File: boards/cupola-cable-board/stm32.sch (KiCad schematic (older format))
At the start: 15 parts, among them J11 SWD, J12 DebugUart, U2 STM32F410CBTx, X1 ECS-3963-120-AU-TR

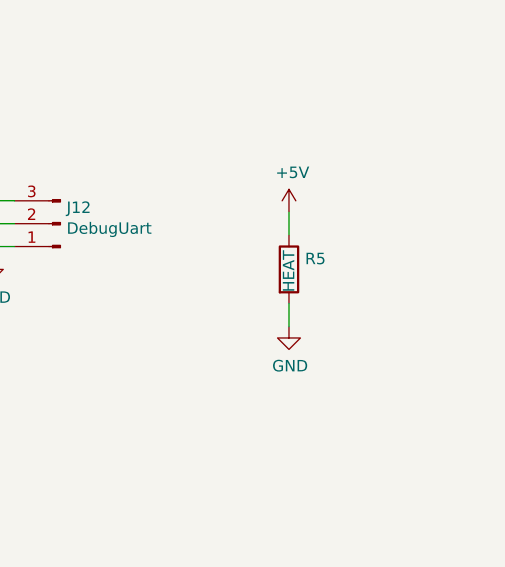
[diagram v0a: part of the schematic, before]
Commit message: cupola_cable_board: 500mA 3.3V regulator, 4 pin connector for magnetic encoder
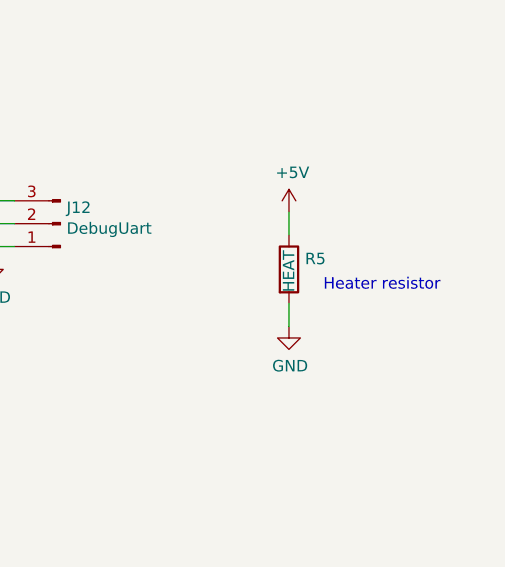
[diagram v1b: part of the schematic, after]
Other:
- note added: "Heater resistor"
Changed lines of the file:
@@
 Wire Wire Line
 	8400 2100 8400 2200
+Text Notes 8550 2050 0    50   ~ 0
+Heater resistor
 $EndSCHEMATC

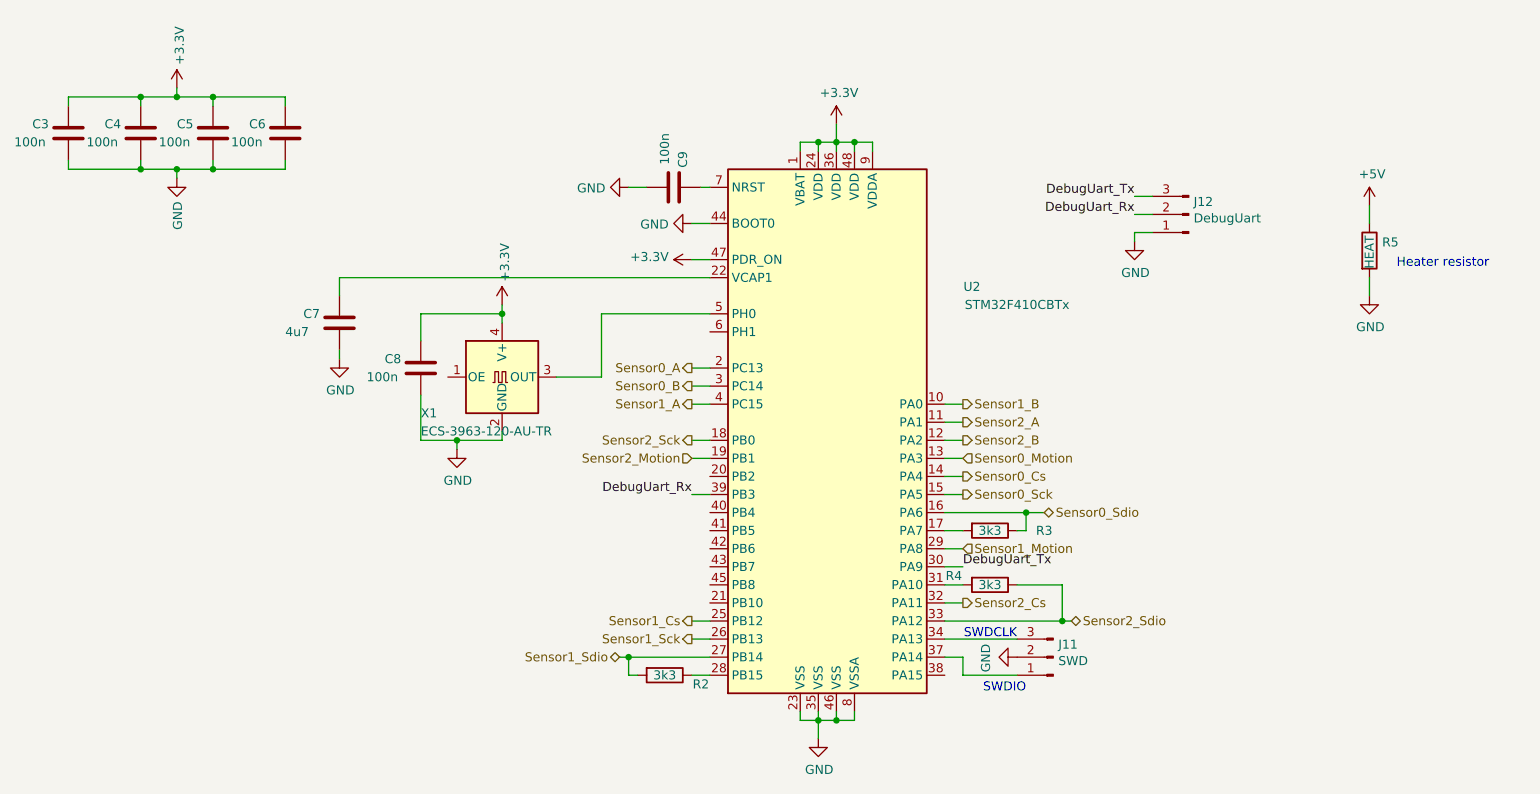
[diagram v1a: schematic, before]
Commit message: cupola board: Swap STM pins for easier layout
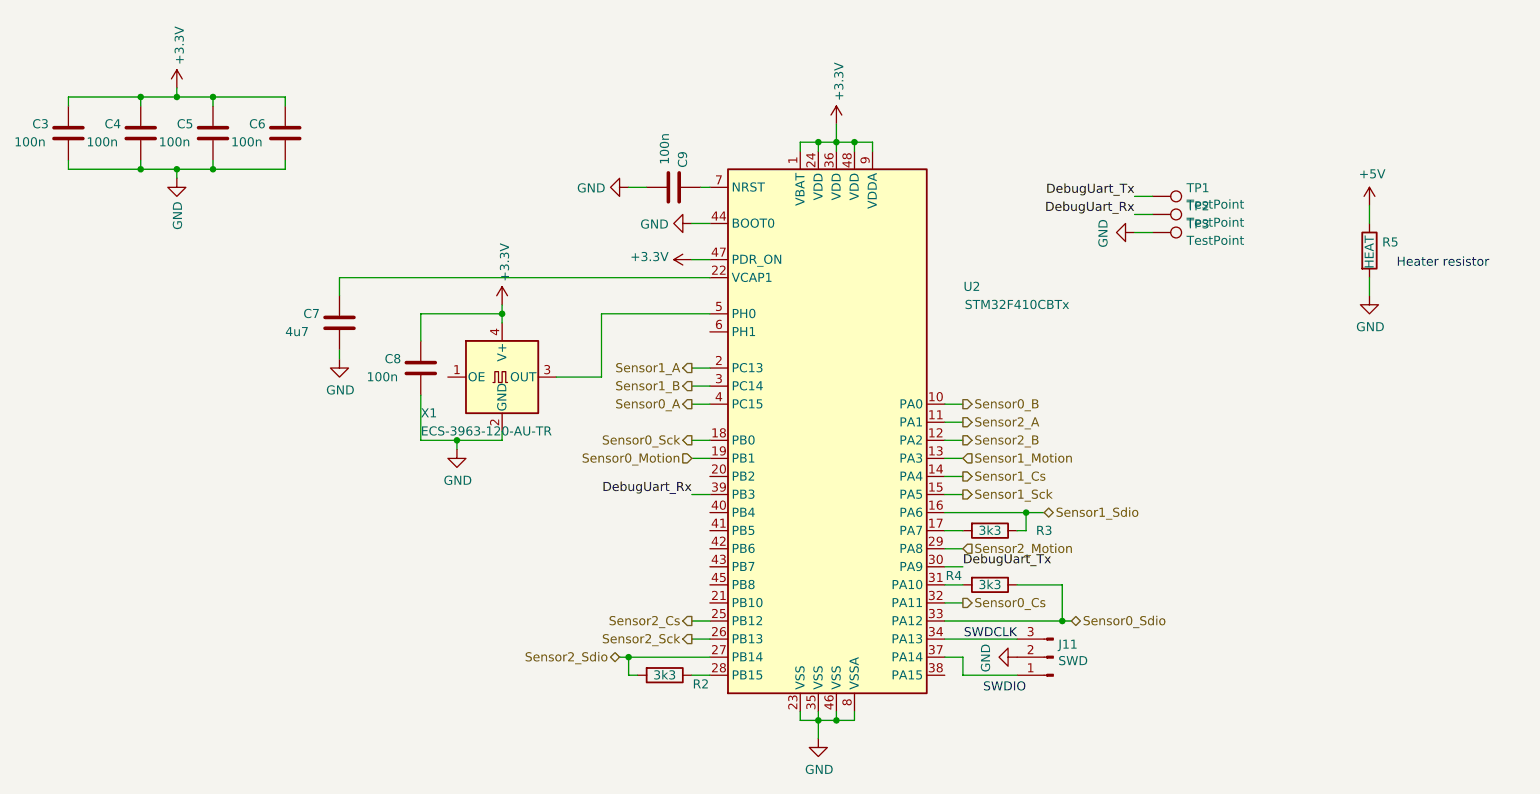
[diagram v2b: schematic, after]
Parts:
- removed J12: DebugUart, symbol Connector:Conn_01x03_Male
- added TP1, TP2, TP3: TestPoint, TestPoint:TestPoint_Pad_D1.5mm, symbol Connector:TestPoint
- J11: footprint (none) -> Connector_PinHeader_2.54mm:PinHeader_1x03_P2.54mm_Vertical
- R2, R3, R4: footprint (none) -> Resistor_SMD:R_0603_1608Metric
- R5: footprint (none) -> Resistor_SMD:R_0805_2012Metric
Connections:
- net DebugUart_Rx: now also TP2.1
- net DebugUart_Tx: now also TP1.1
- net GND: now also TP3.1
- net Sensor0_A: now also U2.4 (PC15); no longer U2.2 (PC13)
- net Sensor0_B: now also U2.10 (PA0); no longer U2.3 (PC14)
- net Sensor0_Cs: now also U2.32 (PA11); no longer U2.14 (PA4)
- net Sensor0_Motion: now also U2.19 (PB1); no longer U2.13 (PA3)
- net Sensor0_Sck: now also U2.18 (PB0); no longer U2.15 (PA5)
- net Sensor0_Sdio: now also R4.1, U2.33 (PA12); no longer R3.1, U2.16 (PA6)
- net Sensor1_A: now also U2.2 (PC13); no longer U2.4 (PC15)
- net Sensor1_B: now also U2.3 (PC14); no longer U2.10 (PA0)
- net Sensor1_Cs: now also U2.14 (PA4); no longer U2.25 (PB12)
- net Sensor1_Motion: now also U2.13 (PA3); no longer U2.29 (PA8)
- net Sensor1_Sck: now also U2.15 (PA5); no longer U2.26 (PB13)
- net Sensor1_Sdio: now also R3.1, U2.16 (PA6); no longer R2.2, U2.27 (PB14)
- net Sensor2_Cs: now also U2.25 (PB12); no longer U2.32 (PA11)
- net Sensor2_Motion: now also U2.29 (PA8); no longer U2.19 (PB1)
- net Sensor2_Sck: now also U2.26 (PB13); no longer U2.18 (PB0)
- net Sensor2_Sdio: now also R2.2, U2.27 (PB14); no longer R4.1, U2.33 (PA12)
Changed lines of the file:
@@
-	1    0    0    -1
-$EndComp
-$Comp
-L power:+3.3V #PWR027
-U 1 1 5C3149FA
-P 5450 1250
-F 0 "#PWR027" H 5450 1100 50  0001 C CNN
-F 1 "+3.3V" H 5465 1423 50  0000 C CNN
-F 2 "" H 5450 1250 50  0001 C CNN
-F 3 "" H 5450 1250 50  0001 C CNN
-	1    5450 1250
 	1    0    0    -1
 $EndComp
@@
 Wire Wire Line
 	4150 2300 4750 2300
+Text HLabel 4650 2800 0    50   Output ~ 0
+Sensor0_A
+Text HLabel 6150 2800 2    50   Output ~ 0
+Sensor0_B
 Text HLabel 4650 2600 0    50   Output ~ 0
-Sensor0_A
-Wire Wire Line
-	4650 2600 4750 2600
+Sensor1_A
 Text HLabel 4650 2700 0    50   Output ~ 0
-Sensor0_B
-Wire Wire Line
-	4750 2700 4650 2700
-Text HLabel 4650 2800 0    50   Output ~ 0
-Sensor1_A
-Wire Wire Line
-	4750 2800 4650 2800
-Text HLabel 6150 2800 2    50   Output ~ 0
 Sensor1_B
-Wire Wire Line
-	6150 2800 6050 2800
 Text HLabel 6150 2900 2    50   Output ~ 0
 Sensor2_A
@@
 Wire Wire Line
 	6150 3000 6050 3000
-Text HLabel 6150 3100 2    50   Input ~ 0
+Text HLabel 4650 3100 0    50   Input ~ 0
 Sensor0_Motion
-Text HLabel 6150 3200 2    50   Output ~ 0
+Text HLabel 6150 3900 2    50   Output ~ 0
 Sensor0_Cs
 Wire Wire Line
@@
 Wire Wire Line
 	6150 3200 6050 3200
-Text HLabel 6150 3300 2    50   Output ~ 0
+Text HLabel 4650 3000 0    50   Output ~ 0
 Sensor0_Sck
-Text HLabel 6600 3400 2    50   BiDi ~ 0
+Text HLabel 6750 4000 2    50   BiDi ~ 0
 Sensor0_Sdio
 $Comp
@@
 F 0 "R3" V 6300 3800 50  0000 C CNN
 F 1 "3k3" V 6300 3500 50  0000 C CNN
-F 2 "" V 6230 3500 50  0001 C CNN
+F 2 "Resistor_SMD:R_0603_1608Metric" V 6230 3500 50  0001 C CNN
 F 3 "~" H 6300 3500 50  0001 C CNN
 	1    6300 3500
@@
 Wire Wire Line
 	6150 3300 6050 3300
-Text HLabel 6150 3600 2    50   Input ~ 0
+Text HLabel 6150 3100 2    50   Input ~ 0
 Sensor1_Motion
 Wire Wire Line
 	6150 3600 6050 3600
-Text HLabel 6150 3900 2    50   Output ~ 0
+Text HLabel 4650 4000 0    50   Output ~ 0
 Sensor2_Cs
 $Comp
@@
 F 0 "R4" V 6250 3600 50  0000 C CNN
 F 1 "3k3" V 6300 3800 50  0000 C CNN
-F 2 "" V 6230 3800 50  0001 C CNN
+F 2 "Resistor_SMD:R_0603_1608Metric" V 6230 3800 50  0001 C CNN
 F 3 "~" H 6300 3800 50  0001 C CNN
 	1    6300 3800
@@
 Wire Wire Line
 	6150 3700 6050 3700
-Text HLabel 6750 4000 2    50   BiDi ~ 0
+Text HLabel 4250 4200 0    50   BiDi ~ 0
 Sensor2_Sdio
 Wire Wire Line
@@
 F 0 "J11" H 6622 4130 50  0000 R CNN
 F 1 "SWD" H 6622 4221 50  0000 R CNN
-F 2 "" H 6650 4200 50  0001 C CNN
+F 2 "Connector_PinHeader_2.54mm:PinHeader_1x03_P2.54mm_Vertical" H 6650 4200 50  0001 C CNN
 F 3 "~" H 6650 4200 50  0001 C CNN
 	1    6650 4200
@@
 Text Notes 6450 4100 2    50   ~ 0
 SWDCLK
-Text HLabel 4650 3000 0    50   Output ~ 0
+Text HLabel 4650 4100 0    50   Output ~ 0
 Sensor2_Sck
 Wire Wire Line
 	4750 3000 4650 3000
-Text HLabel 4650 3100 0    50   Input ~ 0
+Text HLabel 6150 3600 2    50   Input ~ 0
 Sensor2_Motion
 Text Label 4650 3300 2    50   ~ 0
@@
 Wire Wire Line
 	4750 3300 4650 3300
-Text HLabel 4650 4000 0    50   Output ~ 0
+Text HLabel 6150 3200 2    50   Output ~ 0
 Sensor1_Cs
-Text HLabel 4650 4100 0    50   Output ~ 0
+Text HLabel 6150 3300 2    50   Output ~ 0
 Sensor1_Sck
 $Comp
@@
 F 0 "R2" V 4550 4500 50  0000 C CNN
 F 1 "3k3" V 4500 4300 50  0000 C CNN
-F 2 "" V 4430 4300 50  0001 C CNN
+F 2 "Resistor_SMD:R_0603_1608Metric" V 4430 4300 50  0001 C CNN
 F 3 "~" H 4500 4300 50  0001 C CNN
 	1    4500 4300
 	0    1    1    0
 $EndComp
-Text HLabel 4250 4200 0    50   BiDi ~ 0
+Text HLabel 6600 3400 2    50   BiDi ~ 0
 Sensor1_Sdio
 Wire Wire Line
@@
 	4300 4200 4250 4200
 Connection ~ 4300 4200
-$Comp
-L Connector:Conn_01x03_Male J12
-U 1 1 5C39B791
-P 7400 1750
-F 0 "J12" H 7373 1680 50  0000 R CNN
-F 1 "DebugUart" H 7373 1771 50  0000 R CNN
-F 2 "" H 7400 1750 50  0001 C CNN
-F 3 "~" H 7400 1750 50  0001 C CNN
-	1    7400 1750
-	-1   0    0    1
-$EndComp
-$Comp
-L power:GND #PWR029
-U 1 1 5C39BAC6
-P 7100 1900
-F 0 "#PWR029" H 7100 1650 50  0001 C CNN
-F 1 "GND" H 7105 1727 50  0000 C CNN
-F 2 "" H 7100 1900 50  0001 C CNN
-F 3 "" H 7100 1900 50  0001 C CNN
-	1    7100 1900
-	1    0    0    -1
-$EndComp
-Wire Wire Line
-	7100 1850 7100 1900
 Text Label 7100 1650 2    50   ~ 0
 DebugUart_Tx
 Text Label 7100 1750 2    50   ~ 0
 DebugUart_Rx
-Wire Wire Line
-	7100 1650 7200 1650
-Wire Wire Line
-	7100 1750 7200 1750
-Wire Wire Line
-	7100 1850 7200 1850
 $Comp
 L Device:C C4
@@
 F 0 "R5" H 8470 1996 50  0000 L CNN
 F 1 "HEAT" V 8400 1850 50  0000 L CNN
-F 2 "" V 8330 1950 50  0001 C CNN
+F 2 "Resistor_SMD:R_0805_2012Metric" V 8330 1950 50  0001 C CNN
 F 3 "~" H 8400 1950 50  0001 C CNN
 	1    8400 1950
@@
 Text Notes 8550 2050 0    50   ~ 0
 Heater resistor
+$Comp
+L power:+3.3V #PWR0106
+U 1 1 5C3C7090
+P 5450 1250
+F 0 "#PWR0106" H 5450 1100 50  0001 C CNN
+F 1 "+3.3V" V 5465 1378 50  0000 L CNN
+F 2 "" H 5450 1250 50  0001 C CNN
+F 3 "" H 5450 1250 50  0001 C CNN
+	1    5450 1250
+	1    0    0    -1
+$EndComp
+Wire Wire Line
+	4750 2600 4650 2600
+Wire Wire Line
+	4750 2700 4650 2700
+Wire Wire Line
+	4750 2800 4650 2800
+Wire Wire Line
+	6050 2800 6150 2800
+$Comp
+L Connector:TestPoint TP1
+U 1 1 5C43AB33
+P 7200 1650
+F 0 "TP1" V 7154 1838 50  0000 L CNN
+F 1 "TestPoint" V 7245 1838 50  0000 L CNN
+F 2 "TestPoint:TestPoint_Pad_D1.5mm" H 7400 1650 50  0001 C CNN
+F 3 "~" H 7400 1650 50  0001 C CNN
+	1    7200 1650
+	0    1    1    0
+$EndComp
+$Comp
+L Connector:TestPoint TP2
+U 1 1 5C43AB81
+P 7200 1750
+F 0 "TP2" V 7246 1938 50  0000 L CNN
+F 1 "TestPoint" V 7155 1938 50  0000 L CNN
+F 2 "TestPoint:TestPoint_Pad_D1.5mm" H 7400 1750 50  0001 C CNN
+F 3 "~" H 7400 1750 50  0001 C CNN
+	1    7200 1750
+	0    1    -1   0
+$EndComp
+$Comp
+L Connector:TestPoint TP3
+U 1 1 5C43FFBF
+P 7200 1850
+F 0 "TP3" V 7246 2038 50  0000 L CNN
+F 1 "TestPoint" V 7155 2038 50  0000 L CNN
+F 2 "TestPoint:TestPoint_Pad_D1.5mm" H 7400 1850 50  0001 C CNN
+F 3 "~" H 7400 1850 50  0001 C CNN
+	1    7200 1850
+	0    1    -1   0
+$EndComp
+$Comp
+L power:GND #PWR0107
+U 1 1 5C43FFF1
+P 7100 1850
+F 0 "#PWR0107" H 7100 1600 50  0001 C CNN
+F 1 "GND" H 7105 1677 50  0000 C CNN
+F 2 "" H 7100 1850 50  0001 C CNN
+F 3 "" H 7100 1850 50  0001 C CNN
+	1    7100 1850
+	0    1    1    0
+$EndComp
+Wire Wire Line
+	7100 1650 7200 1650
+Wire Wire Line
+	7100 1750 7200 1750
+Wire Wire Line
+	7100 1850 7200 1850
 $EndSCHEMATC

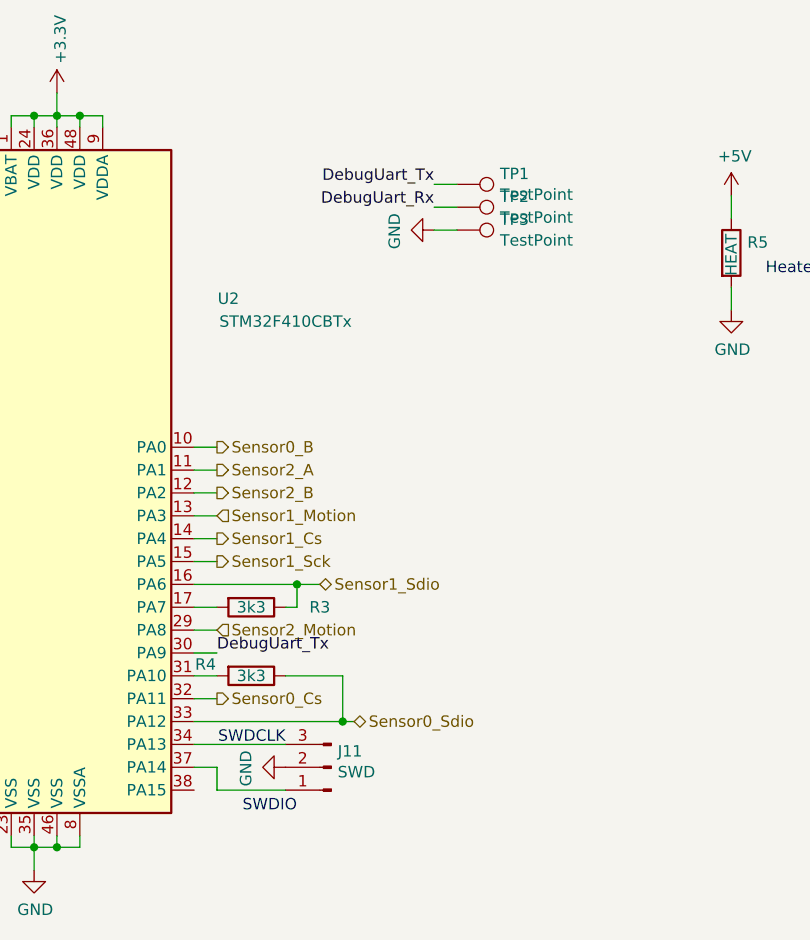
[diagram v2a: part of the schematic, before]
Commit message: [board][cupola-cable-board] Connector placement; Silkscreen
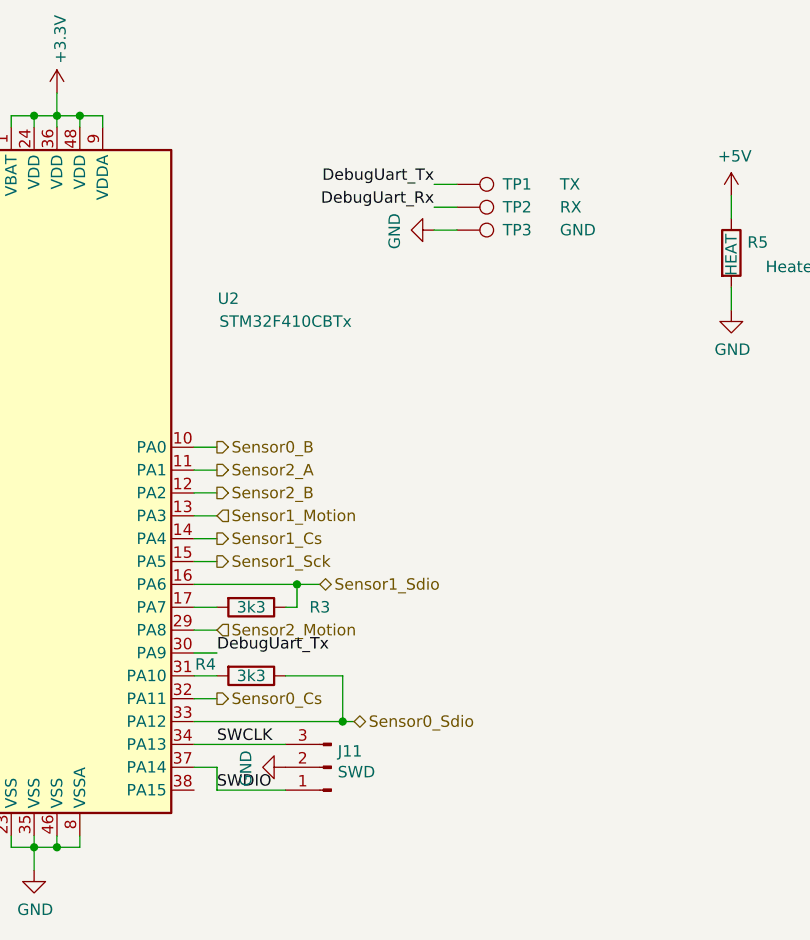
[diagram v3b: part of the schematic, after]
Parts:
- TP1: value TestPoint -> TX; footprint TestPoint:TestPoint_Pad_D1.5mm -> TestPoint:TestPoint_THTPad_D1.5mm_Drill0.7mm
- TP2: value TestPoint -> RX; footprint TestPoint:TestPoint_Pad_D1.5mm -> TestPoint:TestPoint_THTPad_D1.5mm_Drill0.7mm
- TP3: value TestPoint -> GND; footprint TestPoint:TestPoint_Pad_D1.5mm -> TestPoint:TestPoint_THTPad_D1.5mm_Drill0.7mm
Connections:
- net SWCLK: now reaches J11.3 (Pin_3), U2.34 (PA13)
- net SWDIO: now reaches J11.1 (Pin_1), U2.37 (PA14)
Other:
- note removed: "SWDCLK"
- note removed: "SWDIO"
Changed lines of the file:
@@
 Wire Wire Line
 	6150 4300 6450 4300
-Text Notes 6500 4400 2    50   ~ 0
-SWDIO
-Text Notes 6450 4100 2    50   ~ 0
-SWDCLK
 Text HLabel 4650 4100 0    50   Output ~ 0
 Sensor2_Sck
@@
 U 1 1 5C43AB33
 P 7200 1650
-F 0 "TP1" V 7154 1838 50  0000 L CNN
-F 1 "TestPoint" V 7245 1838 50  0000 L CNN
-F 2 "TestPoint:TestPoint_Pad_D1.5mm" H 7400 1650 50  0001 C CNN
+F 0 "TP1" V 7200 1850 50  0000 L CNN
+F 1 "TX" V 7200 2100 50  0000 L CNN
+F 2 "TestPoint:TestPoint_THTPad_D1.5mm_Drill0.7mm" H 7400 1650 50  0001 C CNN
 F 3 "~" H 7400 1650 50  0001 C CNN
 	1    7200 1650
@@
 U 1 1 5C43AB81
 P 7200 1750
-F 0 "TP2" V 7246 1938 50  0000 L CNN
-F 1 "TestPoint" V 7155 1938 50  0000 L CNN
-F 2 "TestPoint:TestPoint_Pad_D1.5mm" H 7400 1750 50  0001 C CNN
+F 0 "TP2" V 7200 1950 50  0000 L CNN
+F 1 "RX" V 7200 2200 50  0000 L CNN
+F 2 "TestPoint:TestPoint_THTPad_D1.5mm_Drill0.7mm" H 7400 1750 50  0001 C CNN
 F 3 "~" H 7400 1750 50  0001 C CNN
 	1    7200 1750
@@
 U 1 1 5C43FFBF
 P 7200 1850
-F 0 "TP3" V 7246 2038 50  0000 L CNN
-F 1 "TestPoint" V 7155 2038 50  0000 L CNN
-F 2 "TestPoint:TestPoint_Pad_D1.5mm" H 7400 1850 50  0001 C CNN
+F 0 "TP3" V 7200 2050 50  0000 L CNN
+F 1 "GND" V 7200 2300 50  0000 L CNN
+F 2 "TestPoint:TestPoint_THTPad_D1.5mm_Drill0.7mm" H 7400 1850 50  0001 C CNN
 F 3 "~" H 7400 1850 50  0001 C CNN
 	1    7200 1850
@@
 Wire Wire Line
 	7100 1850 7200 1850
+Text Label 6150 4100 0    50   ~ 0
+SWCLK
+Text Label 6150 4300 0    50   ~ 0
+SWDIO
 $EndSCHEMATC

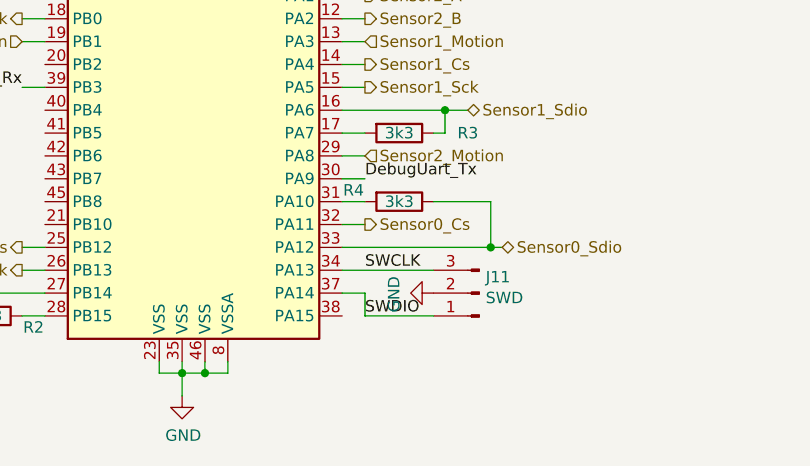
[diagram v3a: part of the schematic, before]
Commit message: [board][cupola-cable-board] Swap SWDIO and SWCLK pins
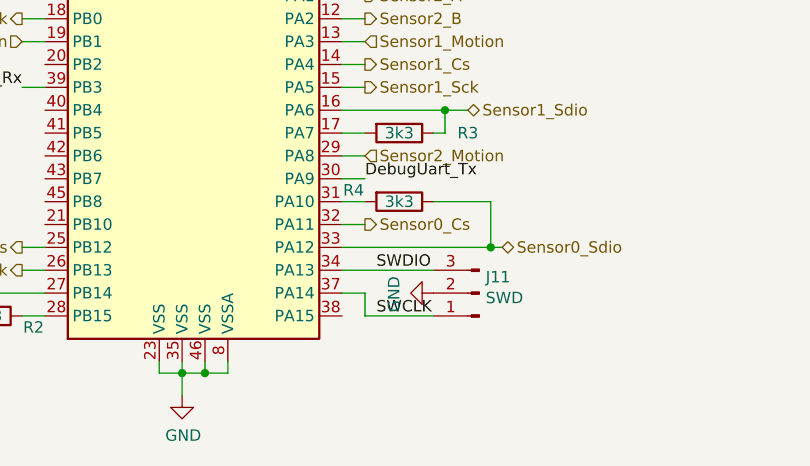
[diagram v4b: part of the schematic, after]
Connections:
- net SWCLK: now also J11.1 (Pin_1), U2.37 (PA14); no longer J11.3 (Pin_3), U2.34 (PA13)
- net SWDIO: now also J11.3 (Pin_3), U2.34 (PA13); no longer J11.1 (Pin_1), U2.37 (PA14)
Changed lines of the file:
@@
 Wire Wire Line
 	7100 1850 7200 1850
-Text Label 6150 4100 0    50   ~ 0
+Text Label 6200 4300 0    50   ~ 0
 SWCLK
-Text Label 6150 4300 0    50   ~ 0
+Text Label 6200 4100 0    50   ~ 0
 SWDIO
 $EndSCHEMATC
